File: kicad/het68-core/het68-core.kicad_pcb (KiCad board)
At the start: 6 copper layers, 160 x 100 mm, 107 parts, among them J1 MIC1, J11 PZ1, J12 PZ2, J13 PZ3, J14 PZ4, J2 MIC2, J3 MIC3, J4 MIC4, J5 MIC5, J6 MIC6, U1 RP2350B, U10 SN65LVDS047, U11 SN65LVDS047, U12 SN65LVDS047, U13 SN65LVDS32, U14 SN65LVDS32, U2 W25Q128JVSIQ, U3 APS6404L, U4 AP2112K-3.3, U5 AP2112K-1.8, U6 DRV8837C, U7 DPS310, U8 SHT40, U9 ADXL355, Y1 12MHz

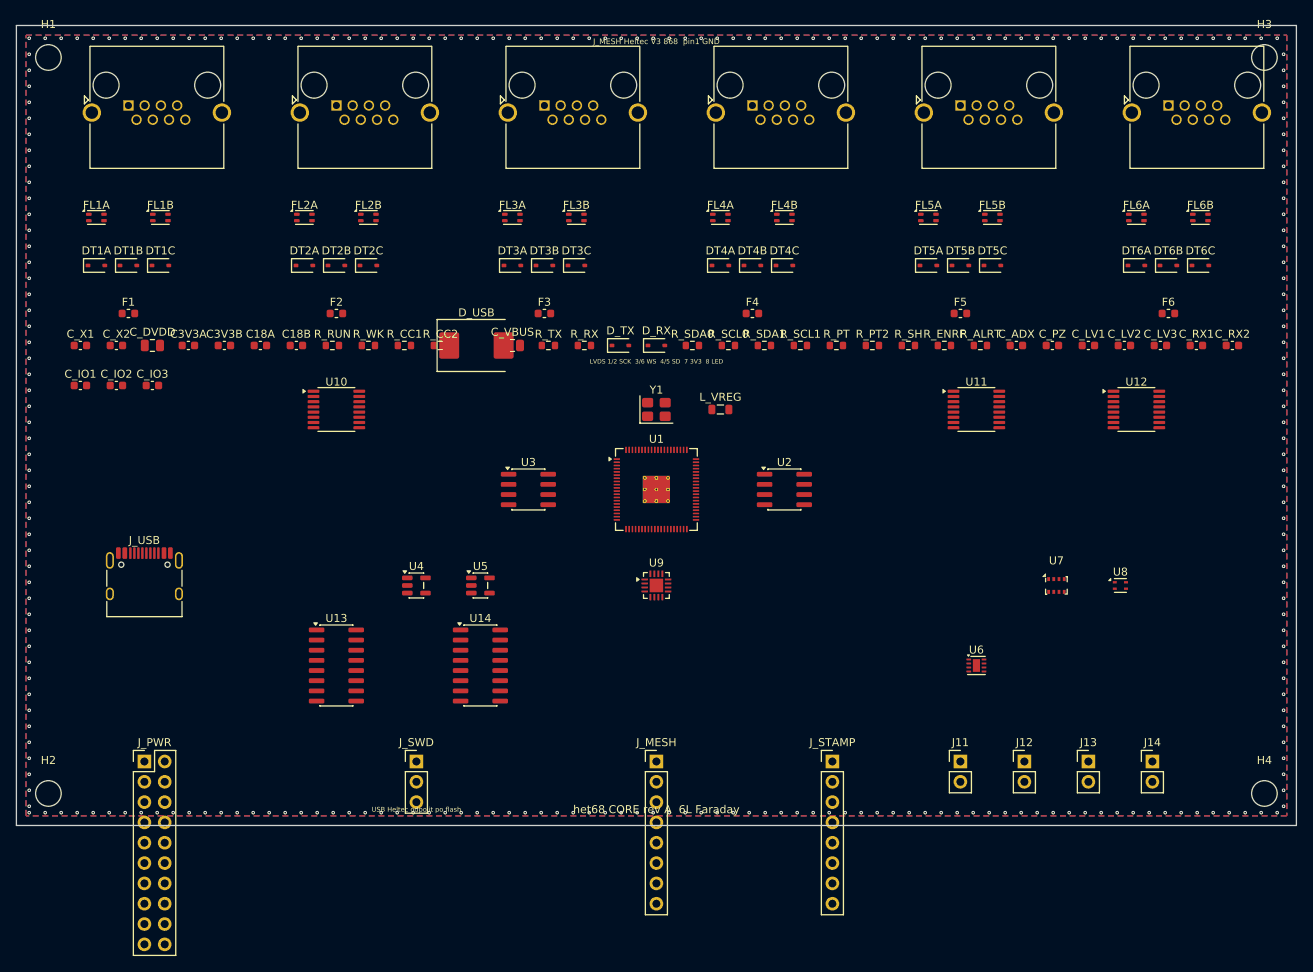
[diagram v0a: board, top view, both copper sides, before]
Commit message: Ship v4.1.0 as a Core+satellite+power kit without the v3 HAT.
LVDS now has 100 ohm receivers, SD common-mode chokes, and 3V3 ferrites for a noisy line; the kit BOM and 3D previews match that schematic.

Co-authored-by: Cursor <cursoragent@cursor.com>
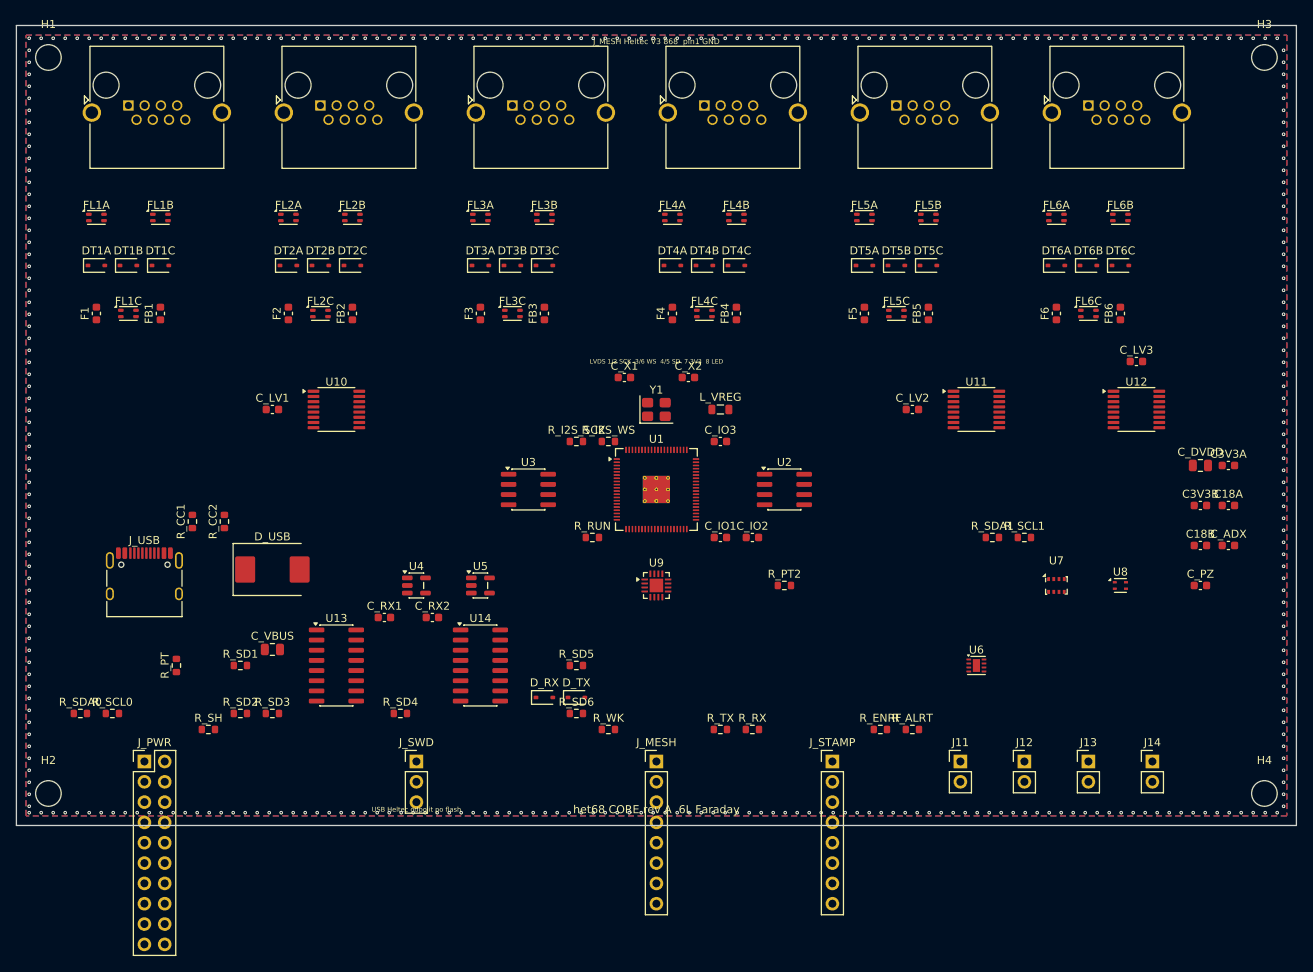
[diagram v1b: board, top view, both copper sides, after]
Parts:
- added FB1: 600R, Inductor_SMD:L_0603_1608Metric, F.Cu at (18.0, 36.0)
- added FB2: 600R, Inductor_SMD:L_0603_1608Metric, F.Cu at (42.0, 36.0)
- added FB3: 600R, Inductor_SMD:L_0603_1608Metric, F.Cu at (66.0, 36.0)
- added FB4: 600R, Inductor_SMD:L_0603_1608Metric, F.Cu at (90.0, 36.0)
- added FB5: 600R, Inductor_SMD:L_0603_1608Metric, F.Cu at (114.0, 36.0)
- added FB6: 600R, Inductor_SMD:L_0603_1608Metric, F.Cu at (138.0, 36.0)
- added FL1C: CMC, Inductor_SMD:L_CommonModeChoke_Coilank_ACM2012, F.Cu at (14.0, 36.0)
- added FL2C: CMC, Inductor_SMD:L_CommonModeChoke_Coilank_ACM2012, F.Cu at (38.0, 36.0)
- added FL3C: CMC, Inductor_SMD:L_CommonModeChoke_Coilank_ACM2012, F.Cu at (62.0, 36.0)
- added FL4C: CMC, Inductor_SMD:L_CommonModeChoke_Coilank_ACM2012, F.Cu at (86.0, 36.0)
- added FL5C: CMC, Inductor_SMD:L_CommonModeChoke_Coilank_ACM2012, F.Cu at (110.0, 36.0)
- added FL6C: CMC, Inductor_SMD:L_CommonModeChoke_Coilank_ACM2012, F.Cu at (134.0, 36.0)
- added R_I2S_SCK: 33, Resistor_SMD:R_0603_1608Metric, F.Cu at (70.0, 52.0)
- added R_I2S_WS: 33, Resistor_SMD:R_0603_1608Metric, F.Cu at (74.0, 52.0)
- added R_SD1: 100, Resistor_SMD:R_0603_1608Metric, F.Cu at (28.0, 80.0)
- added R_SD2: 100, Resistor_SMD:R_0603_1608Metric, F.Cu at (28.0, 86.0)
- added R_SD3: 100, Resistor_SMD:R_0603_1608Metric, F.Cu at (32.0, 86.0)
- added R_SD4: 100, Resistor_SMD:R_0603_1608Metric, F.Cu at (48.0, 86.0)
- added R_SD5: 100, Resistor_SMD:R_0603_1608Metric, F.Cu at (70.0, 80.0)
- added R_SD6: 100, Resistor_SMD:R_0603_1608Metric, F.Cu at (70.0, 86.0)
- moved C_DVDD 131.9 mm to (148.0, 55.0)
- moved C3V3A 130.9 mm to (151.5, 55.0)
- moved C3V3B 123.6 mm to (148.0, 60.0)
- moved C18A 122.6 mm to (151.5, 60.0)
- moved C18B 115.7 mm to (148.0, 65.0)
- moved C_RX1 107.0 mm to (46.0, 74.0)
- moved C_RX2 105.6 mm to (52.0, 74.0)
- moved C_LV1 102.3 mm to (32.0, 48.0)
- moved R_SH 99.8 mm to (24.0, 88.0)
- moved R_PT 91.7 mm to (20.0, 80.0), turned to 90 degrees
- moved R_SCL0 89.7 mm to (12.0, 86.0)
- moved R_SDA0 89.3 mm to (8.00, 86.0)
- moved C_IO1 82.2 mm to (88.0, 64.0)
- moved C_IO2 81.7 mm to (92.0, 64.0)
- moved C_X2 71.6 mm to (84.0, 44.0)
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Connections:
- F1 pad 2: MIC1_3V3 -> MIC1_FB
- F2 pad 2: MIC2_3V3 -> MIC2_FB
- F3 pad 2: MIC3_3V3 -> MIC3_FB
- F4 pad 2: MIC4_3V3 -> MIC4_FB
- F5 pad 2: MIC5_3V3 -> MIC5_FB
- F6 pad 2: MIC6_3V3 -> MIC6_FB
- U1 pad 6: I2S_WS -> I2S_WS_MCU
- U1 pad 7: I2S_SCK -> I2S_SCK_MCU
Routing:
- net GND: vias 254 -> 338

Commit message: Add a Core status LED and three buttons, and fit a 21700 holder.
RESET, BOOT and USER sit on the east edge with one SK6812; the power board uses a Keystone 1122 instead of an 18650 sled. Masks, schematics and JLCPCB gerber zips are in the tree.

Co-authored-by: Cursor <cursoragent@cursor.com>
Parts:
- added C_STAT: 100n, Capacitor_SMD:C_0603_1608Metric, F.Cu at (144.0, 60.0)
- added D_STAT: SK6812, LED_SMD:LED_WS2812B_PLCC4_5.0x5.0mm_P3.2mm, F.Cu at (152.0, 74.0)
- added R_CS: 10k, Resistor_SMD:R_0603_1608Metric, F.Cu at (108.0, 96.0)
- added R_USR: 10k, Resistor_SMD:R_0603_1608Metric, F.Cu at (100.0, 96.0)
- added SW_BOOT: BOOT, Button_Switch_SMD:SW_SPST_PTS645Sx43SMTR92, F.Cu at (152.0, 44.0)
- added SW_RST: RESET, Button_Switch_SMD:SW_SPST_PTS645Sx43SMTR92, F.Cu at (152.0, 28.0)
- added SW_USR: USER, Button_Switch_SMD:SW_SPST_PTS645Sx43SMTR92, F.Cu at (152.0, 60.0)
- moved C_DVDD 140.8 mm to (8.00, 40.0)
- moved C3V3A 139.8 mm to (12.5, 40.0)
- moved C3V3B 132.5 mm to (17.0, 40.0)
- moved C18A 131.5 mm to (21.5, 40.0)
- moved C18B 124.5 mm to (26.0, 40.0)
- moved C_ADX 123.6 mm to (30.5, 40.0)
- moved C_PZ 116.9 mm to (35.0, 40.0)
- moved J_MESH 66.3 mm to (146.0, 86.0), turned to -90 degrees
- moved R_SD5 65.1 mm to (8.00, 60.0)
- moved R_SD6 65.1 mm to (8.00, 66.0)
- moved J_SWD 60.8 mm to (8.00, 48.0)
- moved J_STAMP 46.8 mm to (146.0, 76.0), turned to -90 degrees
- moved R_SCL1 35.4 mm to (100.0, 40.0)
- moved R_SDA1 35.4 mm to (96.0, 40.0)
- moved J11 29.7 mm to (108.0, 64.0)
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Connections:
- U1 pad 46: unconnected-(U1-GPIO37-Pad46) -> STATUS_DIN
- U1 pad 47: unconnected-(U1-GPIO38-Pad47) -> BTN_USER
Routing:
- net GND: vias 338 -> 250
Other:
- board text added: "BOOT"
- board text added: "RST"
- board text added: "USER"

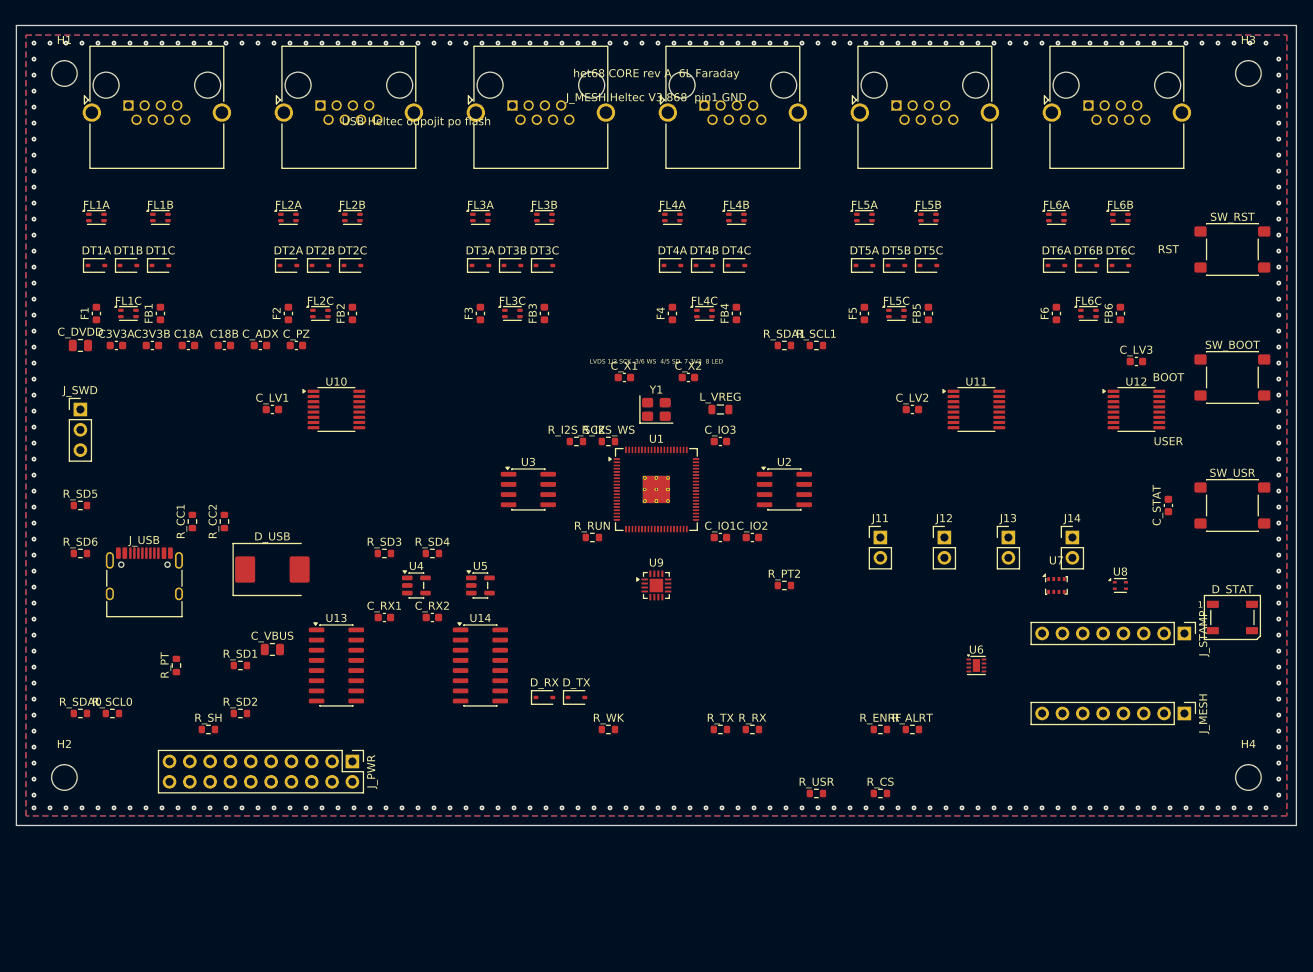
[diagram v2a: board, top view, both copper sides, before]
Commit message: Route signal copper on the five v4 boards and drop tracks that still short.
Core and the satellite have no copper shorts left. QFN-80 fanout and a few LVDS pairs stay open, and the power boards still have overlapping pads from placement.

Co-authored-by: Cursor <cursoragent@cursor.com>
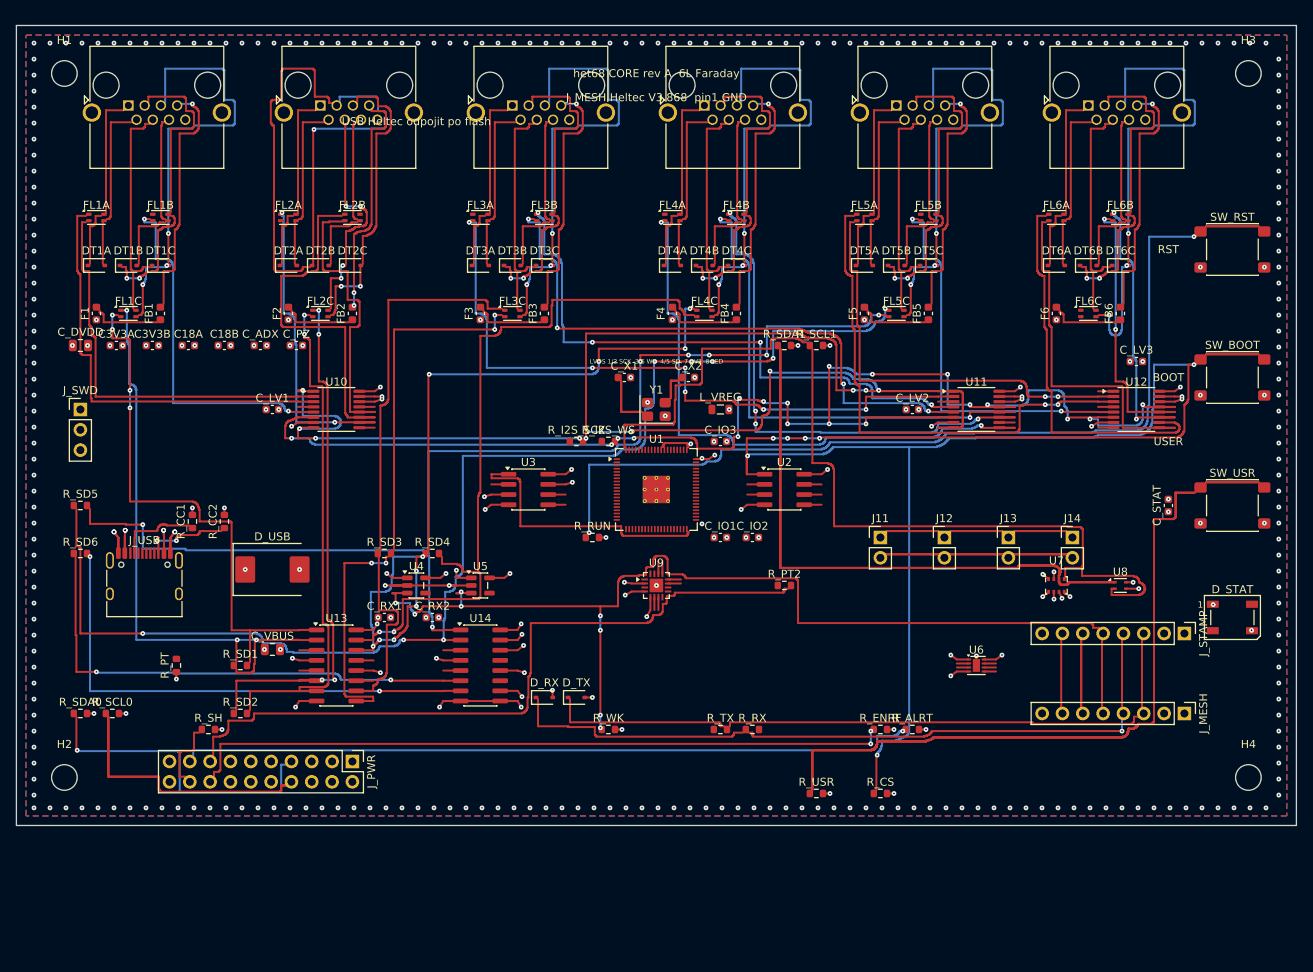
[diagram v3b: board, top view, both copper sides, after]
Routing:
- net I2S_SCK: track 0.00 -> 205.4 mm, vias 0 -> 10
- net QSPI_SS: track 0.00 -> 204.6 mm, vias 0 -> 7
- net BTN_USER: track 0.00 -> 186.3 mm
- net I2S_WS: track 0.00 -> 179.9 mm, vias 0 -> 19
- net SD5_P: track 0.00 -> 165.2 mm, vias 0 -> 8
- net SD5_N: track 0.00 -> 149.4 mm, vias 0 -> 7
- net I2C1_SDA: track 0.00 -> 145.0 mm
- net WAKE_DSP: track 0.00 -> 138.8 mm, vias 0 -> 8
- net RUN: track 0.00 -> 129.0 mm, vias 0 -> 2
- net I2C1_SCL: track 0.00 -> 118.6 mm
- net GND: track 0.00 -> 103.6 mm, vias 250 -> 314
- net SD4_P: track 0.00 -> 102.8 mm, vias 0 -> 10
- net SD4_N: track 0.00 -> 94.2 mm, vias 0 -> 2
- net PT1000_RTN: track 0.00 -> 93.8 mm
- net I2C0_ALERT: track 0.00 -> 93.4 mm, vias 0 -> 1
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
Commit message: Fan out the RP2350B and finish the signal bridges that can leave the package.
Each QFN pin gets a 0.15 mm escape along its axis. The crystal moves off the north row so that corridor exists. Core and the satellite have no new shorts; a few center-row pins and some LVDS nets are still open.

Co-authored-by: Cursor <cursoragent@cursor.com>
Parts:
- moved R_I2S_WS 14.3 mm to (71.0, 66.0)
- moved Y1 8.25 mm to (78.0, 40.0)
- moved L_VREG 6.40 mm to (93.0, 44.0)
- moved C_X1 5.00 mm to (73.0, 40.0)
- moved R_I2S_SCK 4.12 mm to (71.0, 48.0)
- moved C_X2 4.00 mm to (84.0, 40.0)
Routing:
- net +3V3_DIG: track 71.1 -> 474.7 mm, vias 54 -> 86
- net +1V8_AUDIO: track 6.91 -> 262.2 mm, vias 5 -> 13
- net SD6_P: track 64.3 -> 317.1 mm, vias 2 -> 12
- net SD6_N: track 63.8 -> 310.4 mm, vias 2 -> 10
- net +5V_ALWAYS: track 5.57 -> 237.8 mm, vias 3 -> 14
- net PSRAM_SO: track 2.17 -> 175.0 mm, vias 0 -> 10
- net ADC_PT1000: track 1.39 -> 159.0 mm, vias 0 -> 8
- net BURDEN_EN: track 1.39 -> 145.8 mm, vias 0 -> 4
- net PSRAM_CE: track 35.1 -> 177.9 mm, vias 0 -> 12
- net I2S_SD6: track 2.17 -> 134.6 mm, vias 0 -> 12
- net I2S_SD5: track 2.17 -> 133.2 mm, vias 0 -> 10
- net DVDD: track 0.00 -> 130.6 mm, vias 2 -> 6
- net LED6_DIN: track 0.99 -> 129.2 mm, vias 0 -> 3
- net ADC_I: track 1.39 -> 119.6 mm, vias 0 -> 4
- net LED4_DIN: track 0.99 -> 110.2 mm, vias 0 -> 5
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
